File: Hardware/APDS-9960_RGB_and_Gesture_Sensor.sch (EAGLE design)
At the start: 18 parts, among them U1 APDS-9960

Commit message: Created initial layout
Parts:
- R3: value 22 -> 4.7k; device SparkFun-Resistors:22OHM1/10W1%(0603) -> SparkFun-Resistors:4.7KOHM1/10W1%(0603)
- R4: value 4.7k -> 22; device SparkFun-Resistors:4.7KOHM1/10W1%(0603) -> SparkFun-Resistors:22OHM1/10W1%(0603)
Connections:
- net N$2: now also R3.2; no longer R4.2
- net N$3: now also R4.2; no longer R3.2
- net SCL: now also R3.1; no longer R4.1
- net VCC: now also R4.1; no longer R3.1
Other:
- moved on the sheet: R3, R4
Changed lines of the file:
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@@
 <part name="C2" library="SparkFun-Capacitors" deviceset="1.0UF-16V-10%(0603)" device="" value="1.0uF"/>
 <part name="C3" library="SparkFun-Capacitors" deviceset="1.0UF-16V-10%(0603)" device="" value="1.0uF"/>
-<part name="R3" library="SparkFun-Resistors" deviceset="22OHM1/10W1%(0603)" device="" value="22"/>
 <part name="SUPPLY3" library="SparkFun-Aesthetics" deviceset="VCC" device=""/>
-<part name="R4" library="SparkFun-Resistors" deviceset="4.7KOHM1/10W1%(0603)" device="" value="4.7k"/>
 <part name="GND2" library="SparkFun-Aesthetics" deviceset="GND" device=""/>
 <part name="GND3" library="SparkFun-Aesthetics" deviceset="GND" device=""/>
@@
 <part name="LOGO1" library="SparkFun-Aesthetics" deviceset="SFE_LOGO_FLAME" device=".1_INCH"/>
 <part name="LOGO2" library="SparkFun-Aesthetics" deviceset="OSHW-LOGO" device="S"/>
+<part name="R4" library="SparkFun-Resistors" deviceset="22OHM1/10W1%(0603)" device="" value="22"/>
+<part name="R3" library="SparkFun-Resistors" deviceset="4.7KOHM1/10W1%(0603)" device="" value="4.7k"/>
 </parts>
 <sheets>
@@
 <instance part="C2" gate="G$1" x="182.88" y="91.44"/>
 <instance part="C3" gate="G$1" x="172.72" y="116.84"/>
-<instance part="R3" gate="G$1" x="165.1" y="124.46"/>
 <instance part="SUPPLY3" gate="G$1" x="55.88" y="121.92"/>
-<instance part="R4" gate="G$1" x="88.9" y="111.76" rot="R90"/>
 <instance part="GND2" gate="1" x="172.72" y="106.68"/>
 <instance part="GND3" gate="1" x="182.88" y="83.82"/>
@@
 <instance part="LOGO1" gate="G$1" x="132.08" y="20.32"/>
 <instance part="LOGO2" gate="G$1" x="134.62" y="10.16"/>
+<instance part="R4" gate="G$1" x="165.1" y="124.46"/>
+<instance part="R3" gate="G$1" x="88.9" y="111.76" rot="R90"/>
 </instances>
 <busses>
@@
 <wire x1="182.88" y1="99.06" x2="154.94" y2="99.06" width="0.1524" layer="91"/>
 <wire x1="154.94" y1="99.06" x2="154.94" y2="124.46" width="0.1524" layer="91"/>
-<pinref part="R3" gate="G$1" pin="1"/>
 <wire x1="160.02" y1="124.46" x2="154.94" y2="124.46" width="0.1524" layer="91"/>
 <wire x1="154.94" y1="124.46" x2="142.24" y2="124.46" width="0.1524" layer="91"/>
@@
 <wire x1="182.88" y1="96.52" x2="182.88" y2="99.06" width="0.1524" layer="91"/>
 <junction x="182.88" y="99.06"/>
+<pinref part="R4" gate="G$1" pin="1"/>
 </segment>
 </net>
@@
 <wire x1="50.8" y1="104.14" x2="88.9" y2="104.14" width="0.1524" layer="91"/>
 <label x="93.98" y="104.14" size="1.27" layer="95" xref="yes"/>
-<pinref part="R4" gate="G$1" pin="1"/>
 <wire x1="88.9" y1="104.14" x2="93.98" y2="104.14" width="0.1524" layer="91"/>
 <wire x1="88.9" y1="106.68" x2="88.9" y2="104.14" width="0.1524" layer="91"/>
 <junction x="88.9" y="104.14"/>
+<pinref part="R3" gate="G$1" pin="1"/>
 </segment>
 <segment>
@@
 <segment>
 <pinref part="SJ1" gate="G$1" pin="1"/>
-<pinref part="R4" gate="G$1" pin="2"/>
 <wire x1="86.36" y1="119.38" x2="88.9" y2="119.38" width="0.1524" layer="91"/>
 <wire x1="88.9" y1="119.38" x2="88.9" y2="116.84" width="0.1524" layer="91"/>
+<pinref part="R3" gate="G$1" pin="2"/>
 </segment>
 </net>
 <net name="N$3" class="0">
 <segment>
-<pinref part="R3" gate="G$1" pin="2"/>
 <wire x1="170.18" y1="124.46" x2="172.72" y2="124.46" width="0.1524" layer="91"/>
 <pinref part="C3" gate="G$1" pin="1"/>
@@
 <wire x1="182.88" y1="124.46" x2="172.72" y2="124.46" width="0.1524" layer="91"/>
 <junction x="172.72" y="124.46"/>
+<pinref part="R4" gate="G$1" pin="2"/>
 </segment>
 </net>

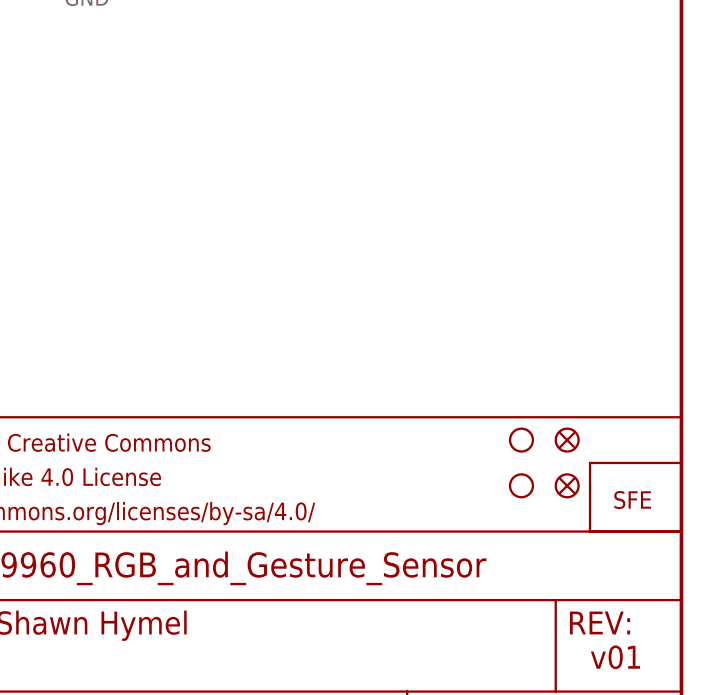
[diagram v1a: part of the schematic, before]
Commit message: Added SS text
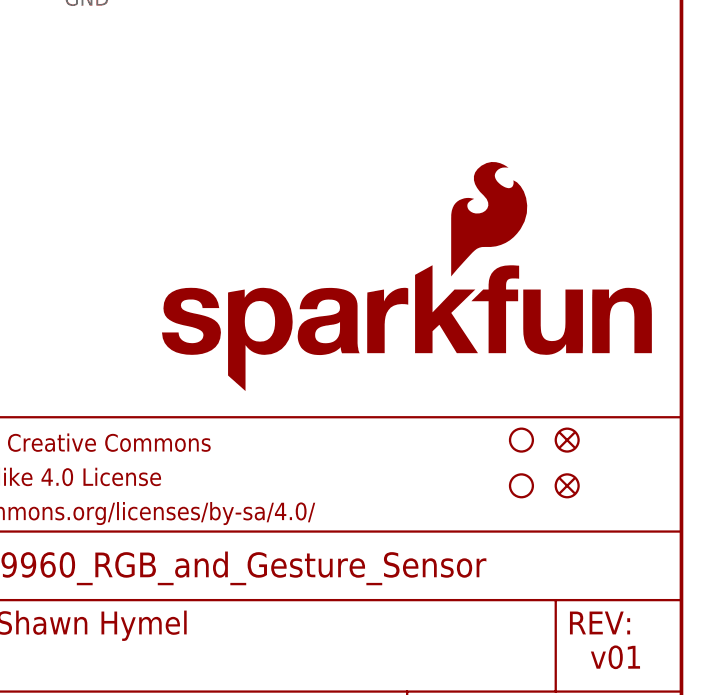
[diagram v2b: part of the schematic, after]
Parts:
- U$1: value SFE_LOGO_NAME_WEB -> SFE_LOGO_NAME_FLAME.1_INCH; device SparkFun-Aesthetics:SFE_LOGO_NAME_WEB -> SparkFun-Aesthetics:SFE_LOGO_NAME_FLAME.1_INCH
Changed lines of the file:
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@@
 <setting verticaltext="up"/>
 </settings>
-<grid distance="0.1" unitdist="inch" unit="inch" style="lines" multiple="1" display="yes" altdistance="0.01" altunitdist="inch" altunit="inch"/>
+<grid distance="0.1" unitdist="inch" unit="inch" style="lines" multiple="1" display="no" altdistance="0.01" altunitdist="inch" altunit="inch"/>
 <layers>
 <layer number="1" name="Top" color="4" fill="1" visible="no" active="no"/>
@@
 <part name="STANDOFF1" library="SparkFun-Electromechanical" deviceset="STAND-OFF" device=""/>
 <part name="STANDOFF2" library="SparkFun-Electromechanical" deviceset="STAND-OFF" device=""/>
-<part name="U$1" library="SparkFun-Aesthetics" deviceset="SFE_LOGO_NAME_WEB" device=""/>
+<part name="U$1" library="SparkFun-Aesthetics" deviceset="SFE_LOGO_NAME_FLAME" device=".1_INCH"/>
 <part name="LOGO1" library="SparkFun-Aesthetics" deviceset="SFE_LOGO_FLAME" device=".1_INCH"/>
 <part name="LOGO2" library="SparkFun-Aesthetics" deviceset="OSHW-LOGO" device="S"/>
@@
 <instance part="STANDOFF1" gate="G$1" x="231.14" y="33.02"/>
 <instance part="STANDOFF2" gate="G$1" x="231.14" y="27.94"/>
-<instance part="U$1" gate="G$1" x="241.3" y="25.4"/>
+<instance part="U$1" gate="G$1" x="190.5" y="38.1"/>
 <instance part="LOGO1" gate="G$1" x="132.08" y="20.32"/>
 <instance part="LOGO2" gate="G$1" x="134.62" y="10.16"/>

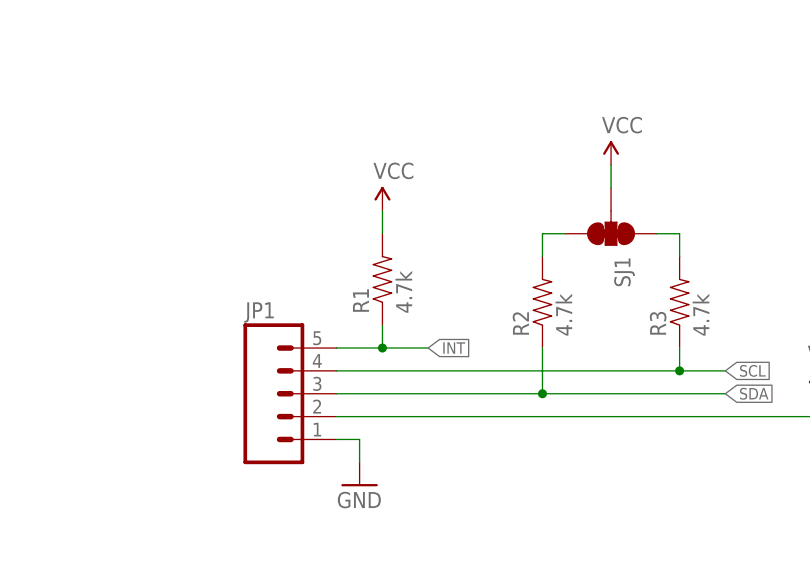
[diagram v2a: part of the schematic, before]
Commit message: Replaced 4.7k INT pullup with 10k
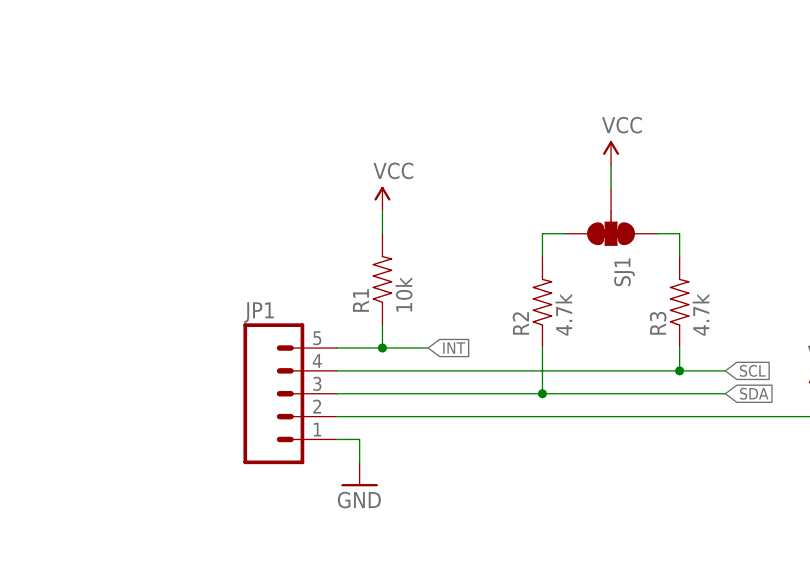
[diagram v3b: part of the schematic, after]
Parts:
- R1: value 4.7k -> 10k; device SparkFun-Resistors:4.7KOHM1/10W1%(0603) -> SparkFun-Resistors:10KOHM1/10W1%(0603)0603
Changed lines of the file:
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@@
 <part name="SUPPLY1" library="SparkFun-Aesthetics" deviceset="VCC" device=""/>
 <part name="GND1" library="SparkFun-Aesthetics" deviceset="GND" device=""/>
-<part name="R1" library="SparkFun-Resistors" deviceset="4.7KOHM1/10W1%(0603)" device="" value="4.7k"/>
+<part name="R1" library="SparkFun-Resistors" deviceset="10KOHM1/10W1%(0603)" device="0603" value="10k"/>
 <part name="R2" library="SparkFun-Resistors" deviceset="4.7KOHM1/10W1%(0603)" device="" value="4.7k"/>
 <part name="SJ1" library="SparkFun-Passives" deviceset="SOLDERJUMPER_2WAY" device="PASTE1&amp;2&amp;3"/>

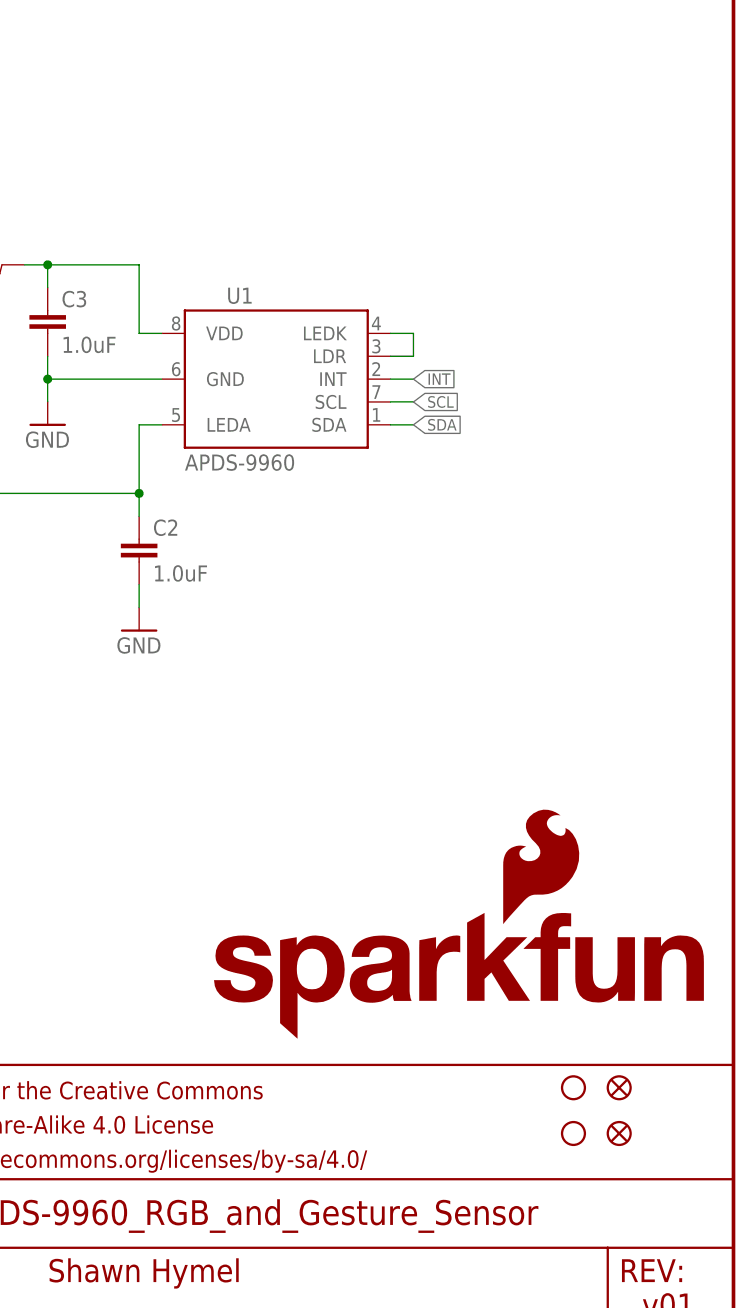
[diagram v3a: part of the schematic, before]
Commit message: Rotated OSHW logo and added I2C address to sch and silk.
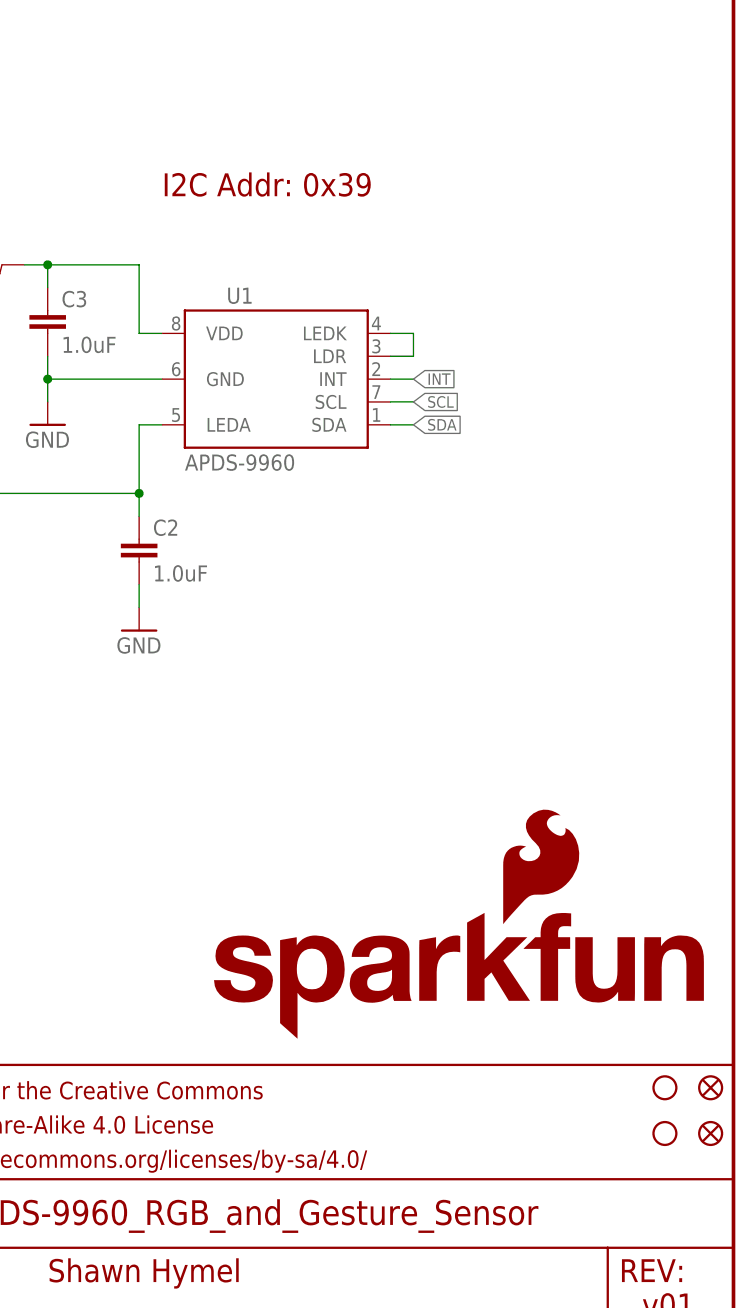
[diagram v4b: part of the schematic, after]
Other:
- note added: "I2C Addr: 0x39"
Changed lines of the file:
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@@
 <setting verticaltext="up"/>
 </settings>
-<grid distance="0.1" unitdist="inch" unit="inch" style="lines" multiple="1" display="no" altdistance="0.01" altunitdist="inch" altunit="inch"/>
+<grid distance="0.1" unitdist="inch" unit="inch" style="lines" multiple="1" display="yes" altdistance="0.01" altunitdist="inch" altunit="inch"/>
 <layers>
 <layer number="1" name="Top" color="4" fill="1" visible="no" active="no"/>
@@
 <text x="172.72" y="12.7" size="2.54" layer="94" align="center-left">Shawn Hymel</text>
 <rectangle x1="79.502" y1="118.872" x2="83.058" y2="119.888" layer="94"/>
+<text x="185.42" y="132.08" size="2.54" layer="94">I2C Addr: 0x39</text>
 </plain>
 <instances>
@@
 <instance part="GND4" gate="1" x="142.24" y="109.22"/>
 <instance part="SUPPLY4" gate="G$1" x="142.24" y="127"/>
-<instance part="FID1" gate="G$1" x="236.22" y="33.02"/>
-<instance part="FID2" gate="G$1" x="236.22" y="27.94"/>
-<instance part="STANDOFF1" gate="G$1" x="231.14" y="33.02"/>
-<instance part="STANDOFF2" gate="G$1" x="231.14" y="27.94"/>
+<instance part="FID1" gate="G$1" x="246.38" y="33.02"/>
+<instance part="FID2" gate="G$1" x="246.38" y="27.94"/>
+<instance part="STANDOFF1" gate="G$1" x="241.3" y="33.02"/>
+<instance part="STANDOFF2" gate="G$1" x="241.3" y="27.94"/>
 <instance part="U$1" gate="G$1" x="190.5" y="38.1"/>
 <instance part="LOGO1" gate="G$1" x="132.08" y="20.32"/>
